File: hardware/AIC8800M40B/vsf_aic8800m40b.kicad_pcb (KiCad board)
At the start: 4 copper layers, 36.8 x 57.2 mm, 86 parts, among them J1 USB_A, J2 USB_C_Receptacle_USB2.0, J3 USB_C_Receptacle_USB2.0, J4 Micro_SD_Card_Det1, J6 Conn_Coaxial, J7 Conn_Coaxial, J8 Conn_02x15_Odd_Even, Q1 S9013, SW1 SW_Push, SW2 SW_Push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

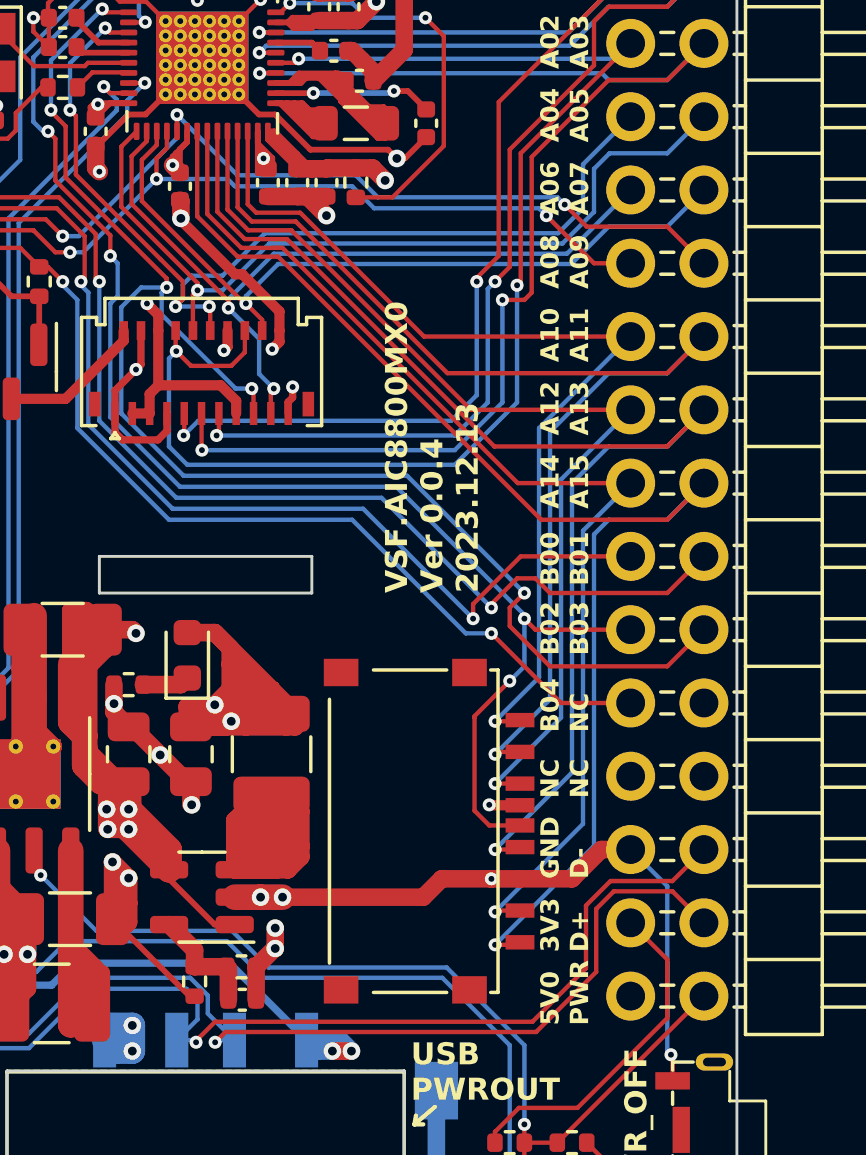
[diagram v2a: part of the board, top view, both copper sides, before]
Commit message: [hardware/aic8800m40b] minor tweak
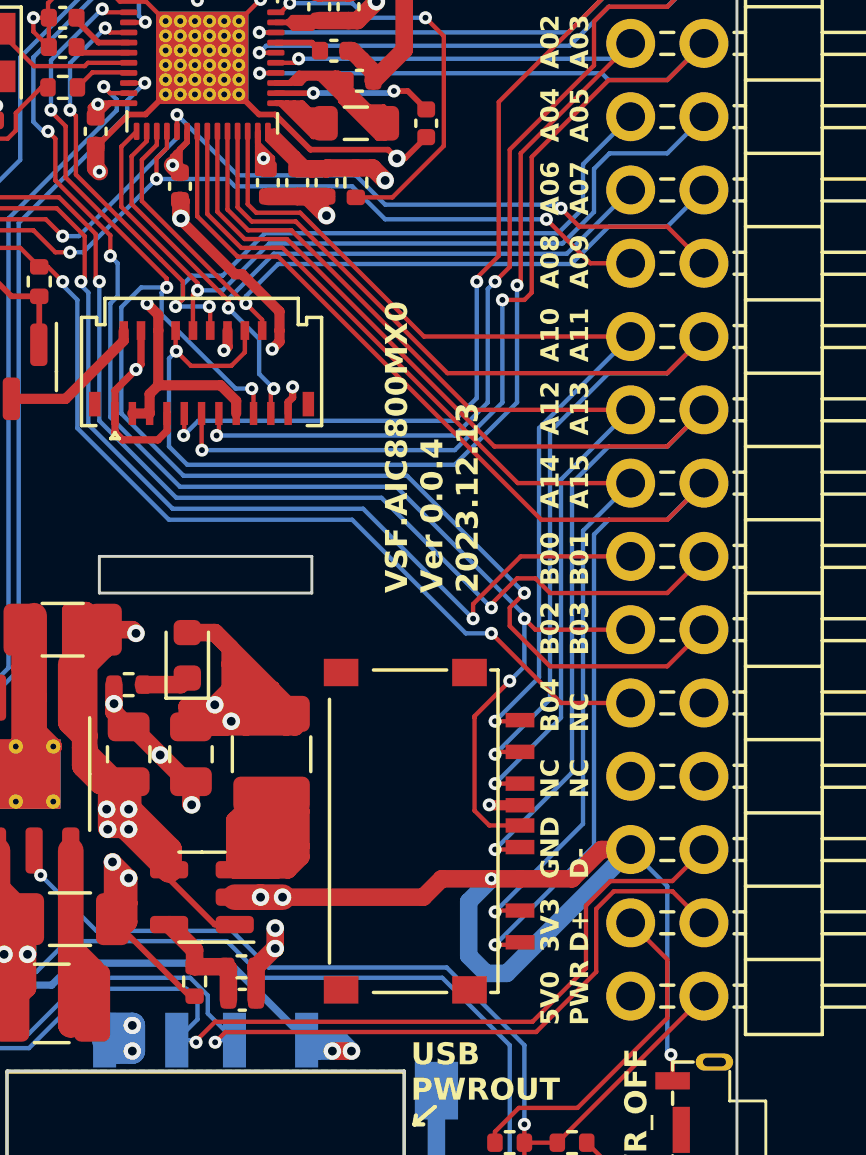
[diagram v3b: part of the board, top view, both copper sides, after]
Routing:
- net GND: track 342.2 -> 347.6 mm
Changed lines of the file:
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@@
   (segment (start 208.153 150.368) (end 210.058 148.463) (width 0.6096) (layer "In1.Cu") (net 1))
   (segment (start 221.5642 113.8428) (end 225.0948 113.8428) (width 0.6096) (layer "In1.Cu") (net 1))
-  (segment (start 235.331 137.541) (end 236.347 136.525) (width 0.889) (layer "In1.Cu") (net 1))
   (segment (start 224.631425 119.892505) (end 224.631425 120.49202) (width 0.3556) (layer "In1.Cu") (net 1))
   (segment (start 212.09 143.4084) (end 212.09 140.97) (width 0.6096) (layer "In1.Cu") (net 1))
@@
   (segment (start 218.3892 136.9568) (end 218.888739 136.9568) (width 0.6096) (layer "In1.Cu") (net 1))
   (segment (start 219.6084 138.176) (end 223.52 138.176) (width 0.6096) (layer "In1.Cu") (net 1))
-  (segment (start 231.521 137.541) (end 235.331 137.541) (width 0.889) (layer "In1.Cu") (net 1))
   (segment (start 215.646 105.1052) (end 215.646 107.696) (width 0.6096) (layer "In1.Cu") (net 1))
   (segment (start 211.182322 143.973178) (end 210.058 145.0975) (width 0.6096) (layer "In1.Cu") (net 1))
@@
   (segment (start 223.012 142.113) (end 223.012 138.684) (width 0.6096) (layer "In1.Cu") (net 1))
   (segment (start 225.115 143.1316) (end 222.4454 140.462) (width 0.254) (layer "B.Cu") (net 1))
+  (segment (start 230.7336 140.208) (end 231.3432 140.8176) (width 0.6096) (layer "B.Cu") (net 1))
   (segment (start 226.0092 143.51) (end 225.4934 143.51) (width 0.6096) (layer "B.Cu") (net 1))
   (segment (start 237.617 143.51) (end 237.617 137.795) (width 0.1524) (layer "B.Cu") (net 1))
+  (segment (start 232.0544 140.8176) (end 236.347 136.525) (width 0.6096) (layer "B.Cu") (net 1))
   (segment (start 226.0092 143.51) (end 226.6696 143.51) (width 0.6096) (layer "B.Cu") (net 1))
   (segment (start 225.4934 143.51) (end 225.115 143.1316) (width 0.6096) (layer "B.Cu") (net 1))
   (segment (start 226.2912 143.1316) (end 225.115 143.1316) (width 0.6096) (layer "B.Cu") (net 1))
   (segment (start 237.744 143.637) (end 237.617 143.51) (width 0.1524) (layer "B.Cu") (net 1))
+  (segment (start 231.3432 140.8176) (end 232.0544 140.8176) (width 0.6096) (layer "B.Cu") (net 1))
+  (segment (start 230.7336 138.3284) (end 230.7336 140.208) (width 0.6096) (layer "B.Cu") (net 1))
+  (segment (start 231.521 137.541) (end 230.7336 138.3284) (width 0.6096) (layer "B.Cu") (net 1))
   (segment (start 216.281 141.224) (end 214.122 141.224) (width 0.254) (layer "B.Cu") (net 1))
   (segment (start 222.4454 140.462) (end 217.043 140.462) (width 0.254) (layer "B.Cu") (net 1))
@@
   (segment (start 220.274 111.633) (end 220.274 112.212) (width 0.1524) (layer "F.Cu") (net 74))
   (segment (start 216.916 115.824) (end 216.408 115.824) (width 0.1524) (layer "F.Cu") (net 74))
+  (segment (start 234.95 116.205) (end 236.347 116.205) (width 0.1524) (layer "F.Cu") (net 74))
   (segment (start 216.408 115.824) (end 215.646 115.062) (width 0.1524) (layer "F.Cu") (net 74))
   (segment (start 215.646 115.062) (end 211.455 115.062) (width 0.1524) (layer "F.Cu") (net 74))
-  (segment (start 233.426 114.554) (end 235.077 116.205) (width 0.1524) (layer "F.Cu") (net 74))
   (segment (start 220.274 112.212) (end 219.9132 112.5728) (width 0.1524) (layer "F.Cu") (net 74))
   (segment (start 211.455 115.062) (end 210.693 115.824) (width 0.1524) (layer "F.Cu") (net 74))
-  (segment (start 235.077 116.205) (end 236.347 116.205) (width 0.1524) (layer "F.Cu") (net 74))
   (segment (start 210.693 115.824) (end 210.693 116.247) (width 0.1524) (layer "F.Cu") (net 74))
+  (segment (start 233.426 114.681) (end 234.95 116.205) (width 0.1524) (layer "F.Cu") (net 74))
   (segment (start 219.9132 112.5728) (end 219.9132 113.284) (width 0.1524) (layer "F.Cu") (net 74))
   (via (at 219.9132 113.284) (size 0.45212) (drill 0.2032) (layers "F.Cu" "B.Cu") (net 74))
   (via (at 216.916 115.824) (size 0.45212) (drill 0.2032) (layers "F.Cu" "B.Cu") (net 74))
-  (via (at 233.426 114.554) (size 0.45212) (drill 0.2032) (layers "F.Cu" "B.Cu") (net 74))
+  (via (at 233.426 114.681) (size 0.45212) (drill 0.2032) (layers "F.Cu" "B.Cu") (net 74))
   (segment (start 216.916 115.824) (end 217.3732 115.824) (width 0.1524) (layer "B.Cu") (net 74))
+  (segment (start 222.631 113.538) (end 222.377 113.284) (width 0.1524) (layer "B.Cu") (net 74))
+  (segment (start 233.426 114.681) (end 227.838 114.681) (width 0.1524) (layer "B.Cu") (net 74))
+  (segment (start 227.838 114.681) (end 226.695 113.538) (width 0.1524) (layer "B.Cu") (net 74))
   (segment (start 222.377 113.284) (end 219.9132 113.284) (width 0.1524) (layer "B.Cu") (net 74))
-  (segment (start 233.426 114.554) (end 233.172 114.3) (width 0.1524) (layer "B.Cu") (net 74))
-  (segment (start 222.631 113.538) (end 222.377 113.284) (width 0.1524) (layer "B.Cu") (net 74))
   (segment (start 226.695 113.538) (end 222.631 113.538) (width 0.1524) (layer "B.Cu") (net 74))
-  (segment (start 233.172 114.3) (end 227.457 114.3) (width 0.1524) (layer "B.Cu") (net 74))
-  (segment (start 227.457 114.3) (end 226.695 113.538) (width 0.1524) (layer "B.Cu") (net 74))
   (segment (start 217.3732 115.824) (end 219.9132 113.284) (width 0.1524) (layer "B.Cu") (net 74))
   (segment (start 220.624 111.633) (end 220.624 111.058822) (width 0.1524) (layer "F.Cu") (net 75))
+  (segment (start 233.934 114.3) (end 234.569 114.935) (width 0.1524) (layer "F.Cu") (net 75))
+  (segment (start 234.569 114.935) (end 237.617 114.935) (width 0.1524) (layer "F.Cu") (net 75))
   (segment (start 220.624 111.058822) (end 220.6244 111.058422) (width 0.2) (layer "F.Cu") (net 75))
+  (segment (start 237.617 114.935) (end 238.887 116.205) (width 0.1524) (layer "F.Cu") (net 75))
   (segment (start 216.662 115.2652) (end 216.0778 114.681) (width 0.1524) (layer "F.Cu") (net 75))
-  (segment (start 234.061 114.173) (end 234.823 114.935) (width 0.1524) (layer "F.Cu") (net 75))
   (segment (start 209.423 115.443) (end 209.423 116.247) (width 0.1524) (layer "F.Cu") (net 75))
-  (segment (start 237.617 114.935) (end 238.887 116.205) (width 0.1524) (layer "F.Cu") (net 75))
   (segment (start 216.0778 114.681) (end 210.185 114.681) (width 0.1524) (layer "F.Cu") (net 75))
-  (segment (start 234.823 114.935) (end 237.617 114.935) (width 0.1524) (layer "F.Cu") (net 75))
   (segment (start 210.185 114.681) (end 209.423 115.443) (width 0.1524) (layer "F.Cu") (net 75))
   (via (at 220.6244 111.058422) (size 0.45212) (drill 0.2032) (layers "F.Cu" "B.Cu") (net 75))
   (via (at 216.662 115.2652) (size 0.45212) (drill 0.2032) (layers "F.Cu" "B.Cu") (net 75))
-  (via (at 234.061 114.173) (size 0.45212) (drill 0.2032) (layers "F.Cu" "B.Cu") (net 75))
+  (via (at 233.934 114.3) (size 0.45212) (drill 0.2032) (layers "F.Cu" "B.Cu") (net 75))
   (segment (start 216.662 115.2652) (end 217.2208 115.2652) (width 0.1524) (layer "B.Cu") (net 75))
-  (segment (start 234.061 114.173) (end 233.807 113.919) (width 0.1524) (layer "B.Cu") (net 75))
   (segment (start 220.6244 111.8616) (end 220.6244 111.058422) (width 0.1524) (layer "B.Cu") (net 75))
+  (segment (start 227.838 114.173) (end 226.822 113.157) (width 0.1524) (layer "B.Cu") (net 75))
+  (segment (start 233.807 114.173) (end 227.838 114.173) (width 0.1524) (layer "B.Cu") (net 75))
+  (segment (start 222.722978 113.157) (end 220.6244 111.058422) (width 0.1524) (layer "B.Cu") (net 75))
+  (segment (start 217.2208 115.2652) (end 220.6244 111.8616) (width 0.1524) (layer "B.Cu") (net 75))
   (segment (start 226.822 113.157) (end 222.722978 113.157) (width 0.1524) (layer "B.Cu") (net 75))
-  (segment (start 227.584 113.919) (end 226.822 113.157) (width 0.1524) (layer "B.Cu") (net 75))
-  (segment (start 217.2208 115.2652) (end 220.6244 111.8616) (width 0.1524) (layer "B.Cu") (net 75))
-  (segment (start 233.807 113.919) (end 227.584 113.919) (width 0.1524) (layer "B.Cu") (net 75))
-  (segment (start 222.722978 113.157) (end 220.6244 111.058422) (width 0.1524) (layer "B.Cu") (net 75))
+  (segment (start 233.934 114.3) (end 233.807 114.173) (width 0.1524) (layer "B.Cu") (net 75))
   (segment (start 224.8408 109.1184) (end 224.7012 109.258) (width 0.1524) (layer "F.Cu") (net 76))
   (segment (start 236.347 108.585) (end 236.474 108.585) (width 0.1524) (layer "F.Cu") (net 76))
@@
   (via (at 220.853 122.174) (size 0.45212) (drill 0.2032) (layers "F.Cu" "B.Cu") (net 78))
   (segment (start 236.347 106.045) (end 234.188 108.204) (width 0.1524) (layer "B.Cu") (net 78))
-  (segment (start 231.013 120.777) (end 230.124 121.666) (width 0.1524) (layer "B.Cu") (net 78))
-  (segment (start 231.013 116.84) (end 231.013 120.777) (width 0.1524) (layer "B.Cu") (net 78))
+  (segment (start 230.2256 121.666) (end 221.361 121.666) (width 0.1524) (layer "B.Cu") (net 78))
   (segment (start 221.361 121.666) (end 220.853 122.174) (width 0.1524) (layer "B.Cu") (net 78))
-  (segment (start 230.124 121.666) (end 221.361 121.666) (width 0.1524) (layer "B.Cu") (net 78))
+  (segment (start 231.013 116.84) (end 231.013 120.8786) (width 0.1524) (layer "B.Cu") (net 78))
   (segment (start 234.188 108.204) (end 223.474422 108.204) (width 0.1524) (layer "B.Cu") (net 78))
+  (segment (start 231.013 120.8786) (end 230.2256 121.666) (width 0.1524) (layer "B.Cu") (net 78))
   (segment (start 229.87 108.331) (end 229.87 112.141) (width 0.1524) (layer "F.Cu") (net 79))
   (segment (start 229.87 112.141) (end 228.09 113.921) (width 0.1524) (layer "F.Cu") (net 79))
